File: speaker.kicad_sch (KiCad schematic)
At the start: 18 parts, among them SW1 SW_DIP_x08

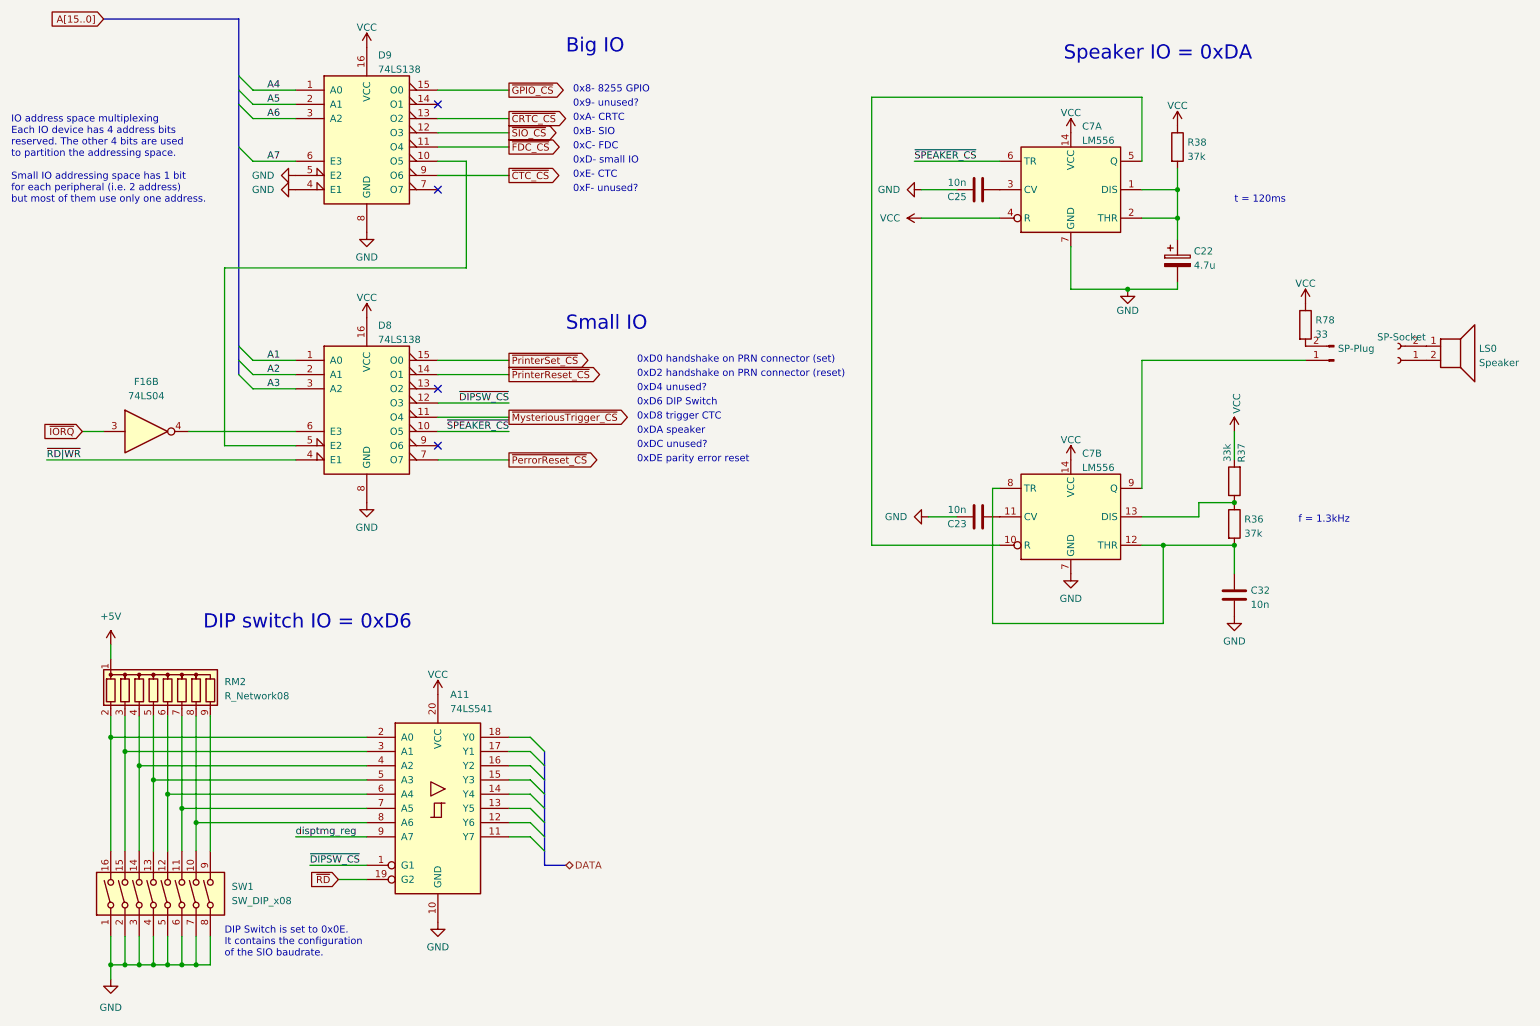
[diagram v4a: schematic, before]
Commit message: Components renaming according to the Uxy convention.
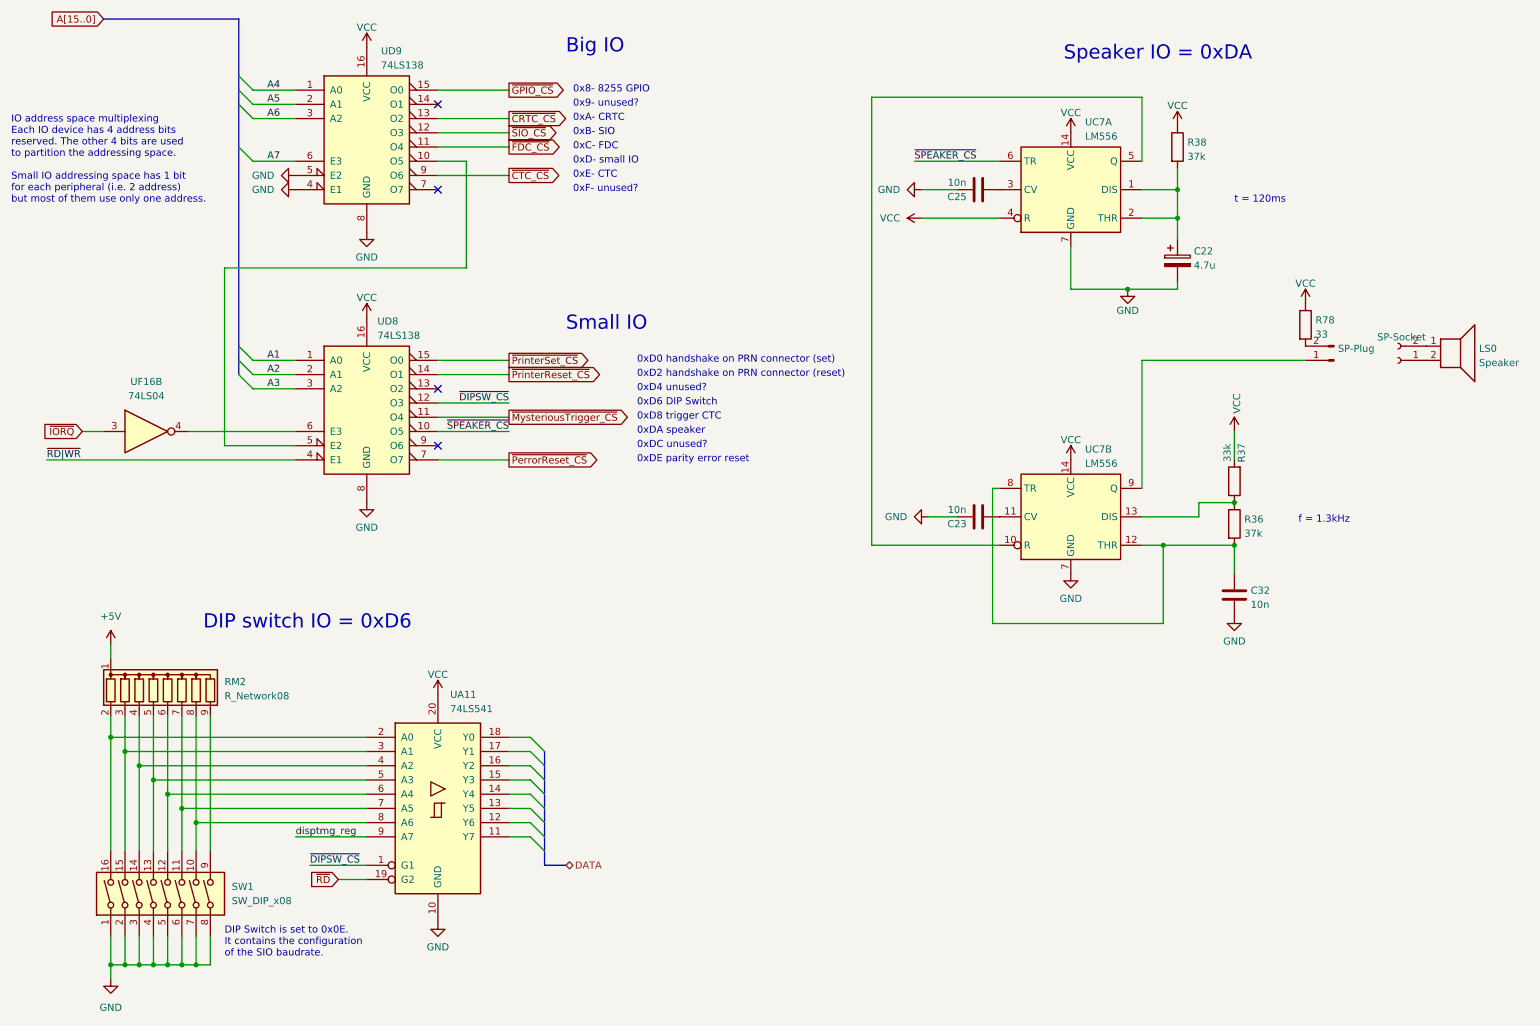
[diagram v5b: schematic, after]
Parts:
- renumbered A11 to UA11, C7 to UC7, D8 to UD8, D9 to UD9, F16 to UF16
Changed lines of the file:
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@@
   )
   (symbol (lib_id "74xx:74LS138") (at 77.47 88.9 0) (unit 1)
-    (in_bom yes) (on_board yes) (dnp no) (fields_autoplaced)
-    (property "Reference" "D8" (at 79.4894 75.0402 0)
-      (effects (font (size 1.27 1.27)) (justify left))
-    )
-    (property "Value" "74LS138" (at 79.4894 77.5771 0)
+    (in_bom yes) (on_board yes) (dnp no)
+    (property "Reference" "UD8" (at 79.375 74.295 0)
+      (effects (font (size 1.27 1.27)) (justify left))
+    )
+    (property "Value" "74LS138" (at 79.375 76.835 0)
       (effects (font (size 1.27 1.27)) (justify left))
     )
@@
       (project "ceda"
         (path "/12a6dbe3-008d-4c5b-88f6-9f1c816060be/ef850a34-fb31-4ec2-8b90-4e6ea535ae17"
-          (reference "D8") (unit 1)
+          (reference "UD8") (unit 1)
         )
       )
@@
   )
   (symbol (lib_id "74xx:74LS138") (at 77.47 40.64 0) (unit 1)
-    (in_bom yes) (on_board yes) (dnp no) (fields_autoplaced)
-    (property "Reference" "D9" (at 79.4894 26.7802 0)
-      (effects (font (size 1.27 1.27)) (justify left))
-    )
-    (property "Value" "74LS138" (at 79.4894 29.3171 0)
+    (in_bom yes) (on_board yes) (dnp no)
+    (property "Reference" "UD9" (at 80.01 26.035 0)
+      (effects (font (size 1.27 1.27)) (justify left))
+    )
+    (property "Value" "74LS138" (at 80.01 28.575 0)
       (effects (font (size 1.27 1.27)) (justify left))
     )
@@
       (project "ceda"
         (path "/12a6dbe3-008d-4c5b-88f6-9f1c816060be/ef850a34-fb31-4ec2-8b90-4e6ea535ae17"
-          (reference "D9") (unit 1)
+          (reference "UD9") (unit 1)
         )
       )
@@
   (symbol (lib_id "74xx:74LS541") (at 90.17 161.29 0) (unit 1)
     (in_bom yes) (on_board yes) (dnp no) (fields_autoplaced)
-    (property "Reference" "A11" (at 92.3641 140.97 0)
+    (property "Reference" "UA11" (at 92.3641 140.97 0)
       (effects (font (size 1.27 1.27)) (justify left))
     )
@@
       (project "ceda"
         (path "/12a6dbe3-008d-4c5b-88f6-9f1c816060be/ef850a34-fb31-4ec2-8b90-4e6ea535ae17"
-          (reference "A11") (unit 1)
+          (reference "UA11") (unit 1)
         )
       )
@@
   (symbol (lib_id "74xx:74LS04") (at 38.1 93.98 0) (unit 2)
     (in_bom yes) (on_board yes) (dnp no) (fields_autoplaced)
-    (property "Reference" "F16" (at 38.1 85.09 0)
+    (property "Reference" "UF16" (at 38.1 85.09 0)
       (effects (font (size 1.27 1.27)))
     )
@@
       (project "ceda"
         (path "/12a6dbe3-008d-4c5b-88f6-9f1c816060be/ef850a34-fb31-4ec2-8b90-4e6ea535ae17"
-          (reference "F16") (unit 2)
+          (reference "UF16") (unit 2)
         )
       )
@@
   )
   (symbol (lib_id "Timer:LM556") (at 203.2 50.8 0) (unit 1)
-    (in_bom yes) (on_board yes) (dnp no) (fields_autoplaced)
-    (property "Reference" "C7" (at 205.2194 39.4802 0)
-      (effects (font (size 1.27 1.27)) (justify left))
-    )
-    (property "Value" "LM556" (at 205.2194 42.0171 0)
+    (in_bom yes) (on_board yes) (dnp no)
+    (property "Reference" "UC7" (at 205.74 38.735 0)
+      (effects (font (size 1.27 1.27)) (justify left))
+    )
+    (property "Value" "LM556" (at 205.74 41.275 0)
       (effects (font (size 1.27 1.27)) (justify left))
     )
@@
       (project "ceda"
         (path "/12a6dbe3-008d-4c5b-88f6-9f1c816060be/ef850a34-fb31-4ec2-8b90-4e6ea535ae17"
-          (reference "C7") (unit 1)
+          (reference "UC7") (unit 1)
         )
       )
@@
   )
   (symbol (lib_id "Timer:LM556") (at 203.2 109.22 0) (unit 2)
-    (in_bom yes) (on_board yes) (dnp no) (fields_autoplaced)
-    (property "Reference" "C7" (at 205.2194 97.9002 0)
-      (effects (font (size 1.27 1.27)) (justify left))
-    )
-    (property "Value" "LM556" (at 205.2194 100.4371 0)
+    (in_bom yes) (on_board yes) (dnp no)
+    (property "Reference" "UC7" (at 205.74 97.155 0)
+      (effects (font (size 1.27 1.27)) (justify left))
+    )
+    (property "Value" "LM556" (at 205.74 99.695 0)
       (effects (font (size 1.27 1.27)) (justify left))
     )
@@
       (project "ceda"
         (path "/12a6dbe3-008d-4c5b-88f6-9f1c816060be/ef850a34-fb31-4ec2-8b90-4e6ea535ae17"
-          (reference "C7") (unit 2)
-        )
-      )
+          (reference "UC7") (unit 2)
+        )
+      )

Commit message: VCC -> +5V
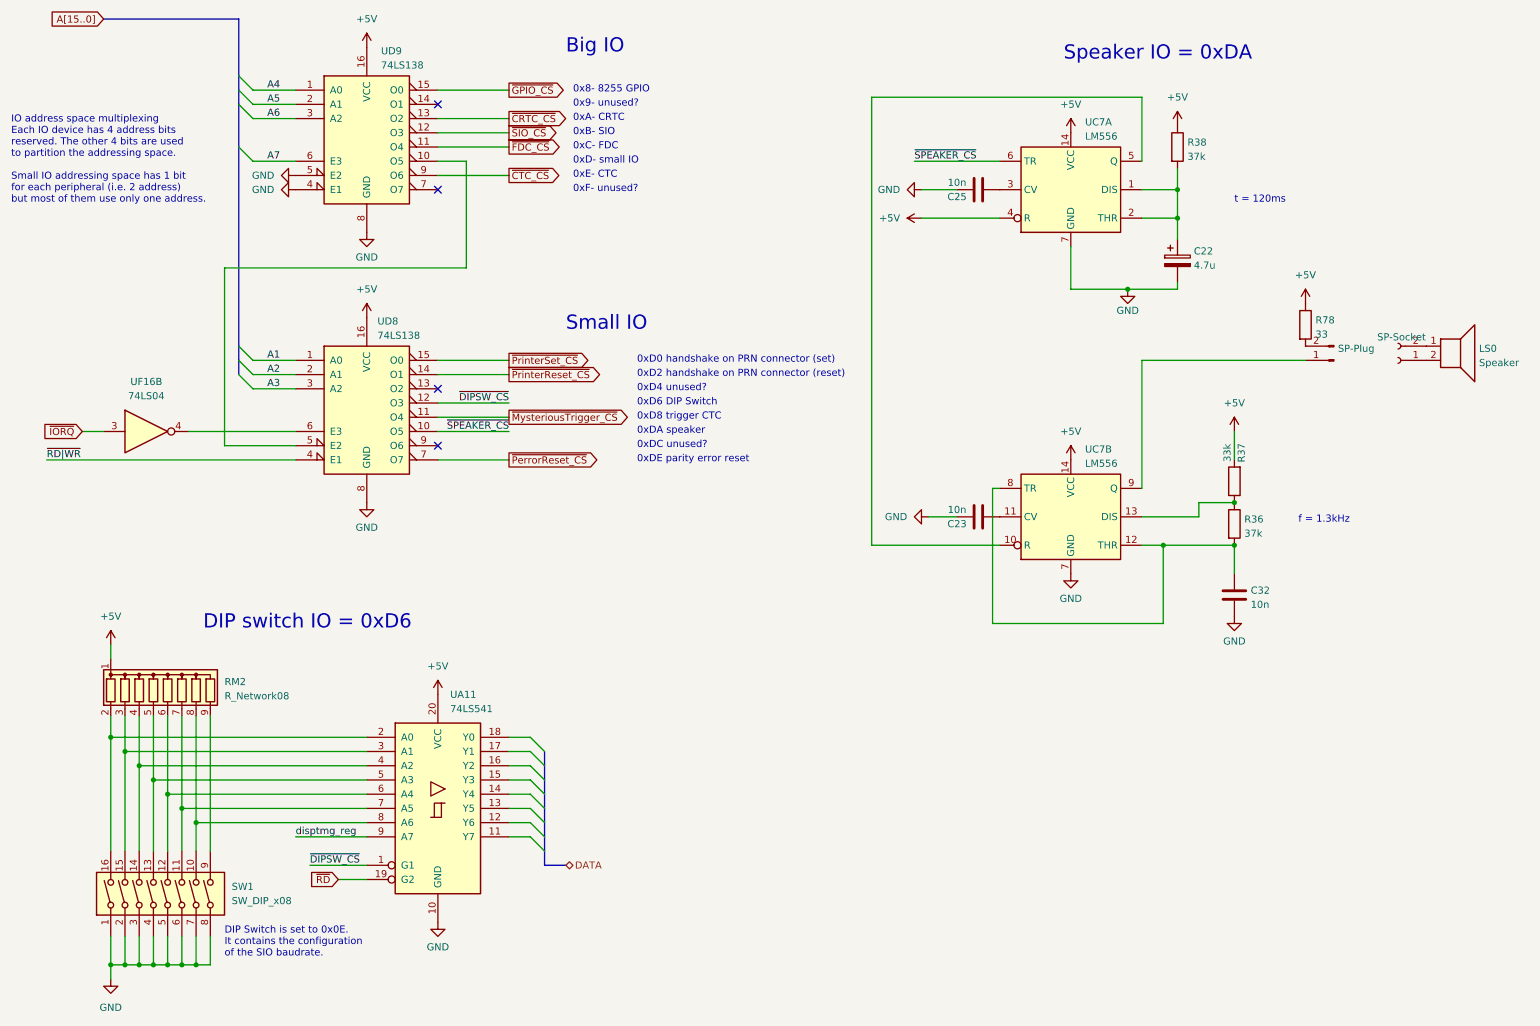
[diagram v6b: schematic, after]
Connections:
- net VCC is gone; now on net +5V: R37.2, R38.1, R78.1, UA11.20 (VCC), UC7.14 (VCC), UC7.14 (VCC), UC7.4 (R), UD8.16 (VCC), UD9.16 (VCC)
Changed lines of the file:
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@@
     )
   )
-  (symbol (lib_id "power:VCC") (at 203.2 40.64 0) (unit 1)
-    (in_bom yes) (on_board yes) (dnp no) (fields_autoplaced)
-    (property "Reference" "#PWR0158" (at 203.2 44.45 0)
-      (effects (font (size 1.27 1.27)) hide)
-    )
-    (property "Value" "VCC" (at 203.2 37.0642 0)
+  (symbol (lib_id "power:+5V") (at 203.2 40.64 0) (unit 1)
+    (in_bom yes) (on_board yes) (dnp no) (fields_autoplaced)
+    (property "Reference" "#PWR?" (at 203.2 44.45 0)
+      (effects (font (size 1.27 1.27)) hide)
+    )
+    (property "Value" "+5V" (at 203.2 35.56 0)
       (effects (font (size 1.27 1.27)))
     )
@@
       (project "ceda"
         (path "/12a6dbe3-008d-4c5b-88f6-9f1c816060be/ef850a34-fb31-4ec2-8b90-4e6ea535ae17"
-          (reference "#PWR0158") (unit 1)
+          (reference "#PWR?") (unit 1)
         )
       )
@@
     )
   )
-  (symbol (lib_id "power:VCC") (at 77.47 73.66 0) (unit 1)
-    (in_bom yes) (on_board yes) (dnp no) (fields_autoplaced)
-    (property "Reference" "#PWR0154" (at 77.47 77.47 0)
-      (effects (font (size 1.27 1.27)) hide)
-    )
-    (property "Value" "VCC" (at 77.47 70.0842 0)
+  (symbol (lib_id "power:+5V") (at 77.47 73.66 0) (unit 1)
+    (in_bom yes) (on_board yes) (dnp no) (fields_autoplaced)
+    (property "Reference" "#PWR?" (at 77.47 77.47 0)
+      (effects (font (size 1.27 1.27)) hide)
+    )
+    (property "Value" "+5V" (at 77.47 68.58 0)
       (effects (font (size 1.27 1.27)))
     )
@@
       (project "ceda"
         (path "/12a6dbe3-008d-4c5b-88f6-9f1c816060be/ef850a34-fb31-4ec2-8b90-4e6ea535ae17"
-          (reference "#PWR0154") (unit 1)
+          (reference "#PWR?") (unit 1)
         )
       )
@@
     )
   )
-  (symbol (lib_id "power:VCC") (at 77.47 25.4 0) (unit 1)
-    (in_bom yes) (on_board yes) (dnp no) (fields_autoplaced)
-    (property "Reference" "#PWR0152" (at 77.47 29.21 0)
-      (effects (font (size 1.27 1.27)) hide)
-    )
-    (property "Value" "VCC" (at 77.47 21.8242 0)
+  (symbol (lib_id "power:+5V") (at 77.47 25.4 0) (unit 1)
+    (in_bom yes) (on_board yes) (dnp no) (fields_autoplaced)
+    (property "Reference" "#PWR?" (at 77.47 29.21 0)
+      (effects (font (size 1.27 1.27)) hide)
+    )
+    (property "Value" "+5V" (at 77.47 20.32 0)
       (effects (font (size 1.27 1.27)))
     )
@@
       (project "ceda"
         (path "/12a6dbe3-008d-4c5b-88f6-9f1c816060be/ef850a34-fb31-4ec2-8b90-4e6ea535ae17"
-          (reference "#PWR0152") (unit 1)
+          (reference "#PWR?") (unit 1)
         )
       )
@@
     )
   )
-  (symbol (lib_id "power:VCC") (at 90.17 140.97 0) (unit 1)
-    (in_bom yes) (on_board yes) (dnp no) (fields_autoplaced)
-    (property "Reference" "#PWR066" (at 90.17 144.78 0)
-      (effects (font (size 1.27 1.27)) hide)
-    )
-    (property "Value" "VCC" (at 90.17 137.3942 0)
+  (symbol (lib_id "power:+5V") (at 90.17 140.97 0) (unit 1)
+    (in_bom yes) (on_board yes) (dnp no) (fields_autoplaced)
+    (property "Reference" "#PWR?" (at 90.17 144.78 0)
+      (effects (font (size 1.27 1.27)) hide)
+    )
+    (property "Value" "+5V" (at 90.17 135.89 0)
       (effects (font (size 1.27 1.27)))
     )
@@
       (project "ceda"
         (path "/12a6dbe3-008d-4c5b-88f6-9f1c816060be/ef850a34-fb31-4ec2-8b90-4e6ea535ae17"
-          (reference "#PWR066") (unit 1)
+          (reference "#PWR?") (unit 1)
         )
       )
@@
     )
   )
-  (symbol (lib_id "power:VCC") (at 203.2 99.06 0) (unit 1)
-    (in_bom yes) (on_board yes) (dnp no) (fields_autoplaced)
-    (property "Reference" "#PWR0146" (at 203.2 102.87 0)
-      (effects (font (size 1.27 1.27)) hide)
-    )
-    (property "Value" "VCC" (at 203.2 95.4842 0)
+  (symbol (lib_id "power:+5V") (at 203.2 99.06 0) (unit 1)
+    (in_bom yes) (on_board yes) (dnp no) (fields_autoplaced)
+    (property "Reference" "#PWR?" (at 203.2 102.87 0)
+      (effects (font (size 1.27 1.27)) hide)
+    )
+    (property "Value" "+5V" (at 203.2 93.98 0)
       (effects (font (size 1.27 1.27)))
     )
@@
       (project "ceda"
         (path "/12a6dbe3-008d-4c5b-88f6-9f1c816060be/ef850a34-fb31-4ec2-8b90-4e6ea535ae17"
-          (reference "#PWR0146") (unit 1)
-        )
-      )
-    )
-  )
-  (symbol (lib_id "power:VCC") (at 176.53 55.88 90) (unit 1)
-    (in_bom yes) (on_board yes) (dnp no) (fields_autoplaced)
-    (property "Reference" "#PWR0156" (at 180.34 55.88 0)
-      (effects (font (size 1.27 1.27)) hide)
-    )
-    (property "Value" "VCC" (at 172.72 55.88 90)
+          (reference "#PWR?") (unit 1)
+        )
+      )
+    )
+  )
+  (symbol (lib_id "power:+5V") (at 176.53 55.88 90) (unit 1)
+    (in_bom yes) (on_board yes) (dnp no) (fields_autoplaced)
+    (property "Reference" "#PWR?" (at 180.34 55.88 0)
+      (effects (font (size 1.27 1.27)) hide)
+    )
+    (property "Value" "+5V" (at 172.72 55.88 90)
       (effects (font (size 1.27 1.27)) (justify left))
     )
@@
       (project "ceda"
         (path "/12a6dbe3-008d-4c5b-88f6-9f1c816060be/ef850a34-fb31-4ec2-8b90-4e6ea535ae17"
-          (reference "#PWR0156") (unit 1)
-        )
-      )
-    )
-  )
-  (symbol (lib_id "power:VCC") (at 222.25 39.37 0) (unit 1)
-    (in_bom yes) (on_board yes) (dnp no) (fields_autoplaced)
-    (property "Reference" "#PWR0159" (at 222.25 43.18 0)
-      (effects (font (size 1.27 1.27)) hide)
-    )
-    (property "Value" "VCC" (at 222.25 35.7942 0)
+          (reference "#PWR?") (unit 1)
+        )
+      )
+    )
+  )
+  (symbol (lib_id "power:+5V") (at 222.25 39.37 0) (unit 1)
+    (in_bom yes) (on_board yes) (dnp no) (fields_autoplaced)
+    (property "Reference" "#PWR?" (at 222.25 43.18 0)
+      (effects (font (size 1.27 1.27)) hide)
+    )
+    (property "Value" "+5V" (at 222.25 34.29 0)
       (effects (font (size 1.27 1.27)))
     )
@@
       (project "ceda"
         (path "/12a6dbe3-008d-4c5b-88f6-9f1c816060be/ef850a34-fb31-4ec2-8b90-4e6ea535ae17"
-          (reference "#PWR0159") (unit 1)
+          (reference "#PWR?") (unit 1)
         )
       )
@@
     )
   )
-  (symbol (lib_id "power:VCC") (at 232.41 93.98 0) (unit 1)
-    (in_bom yes) (on_board yes) (dnp no) (fields_autoplaced)
-    (property "Reference" "#PWR0145" (at 232.41 97.79 0)
-      (effects (font (size 1.27 1.27)) hide)
-    )
-    (property "Value" "VCC" (at 232.8438 90.805 90)
-      (effects (font (size 1.27 1.27)) (justify left))
+  (symbol (lib_id "power:+5V") (at 232.41 93.98 0) (unit 1)
+    (in_bom yes) (on_board yes) (dnp no) (fields_autoplaced)
+    (property "Reference" "#PWR?" (at 232.41 97.79 0)
+      (effects (font (size 1.27 1.27)) hide)
+    )
+    (property "Value" "+5V" (at 232.41 88.9 0)
+      (effects (font (size 1.27 1.27)))
     )
     (property "Footprint" "" (at 232.41 93.98 0)
@@
       (project "ceda"
         (path "/12a6dbe3-008d-4c5b-88f6-9f1c816060be/ef850a34-fb31-4ec2-8b90-4e6ea535ae17"
-          (reference "#PWR0145") (unit 1)
+          (reference "#PWR?") (unit 1)
         )
       )
@@
     )
   )
-  (symbol (lib_id "power:VCC") (at 245.11 71.12 0) (unit 1)
-    (in_bom yes) (on_board yes) (dnp no) (fields_autoplaced)
-    (property "Reference" "#PWR0149" (at 245.11 74.93 0)
-      (effects (font (size 1.27 1.27)) hide)
-    )
-    (property "Value" "VCC" (at 245.11 67.5442 0)
+  (symbol (lib_id "power:+5V") (at 245.11 71.12 0) (unit 1)
+    (in_bom yes) (on_board yes) (dnp no) (fields_autoplaced)
+    (property "Reference" "#PWR?" (at 245.11 74.93 0)
+      (effects (font (size 1.27 1.27)) hide)
+    )
+    (property "Value" "+5V" (at 245.11 66.04 0)
       (effects (font (size 1.27 1.27)))
     )
@@
       (project "ceda"
         (path "/12a6dbe3-008d-4c5b-88f6-9f1c816060be/ef850a34-fb31-4ec2-8b90-4e6ea535ae17"
-          (reference "#PWR0149") (unit 1)
-        )
-      )
+          (reference "#PWR?") (unit 1)
+        )
+      )

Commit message: Notes in kicad's sheet text blocks
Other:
- company: (none) -> Logic Systems Int'l Inc
- title: (none) -> CEDA - Sanco 8003 schematics
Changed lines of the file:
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@@
 (kicad_sch (version 20230121) (generator eeschema)
   (paper "A4")
+  (title_block
+    (title "CEDA - Sanco 8003 schematics")
+    (rev "05")
+    (company "Logic Systems Int'l Inc")
+    (comment 1 "reversed by RetrOfficina - retrofficina.glgprograms.it")
+    (comment 3 "Decode the Z80 I/O addressing space")
+    (comment 4 "I/O Space")
+  )
   (junction (at 44.45 161.29) (diameter 0) (color 0 0 0 0)
   )
